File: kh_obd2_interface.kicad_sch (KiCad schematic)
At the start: 8 parts, among them J1 OBD2, Q1 CSD18540Q5B, U1 LM74500-Q1, U2 TVS2700DRV

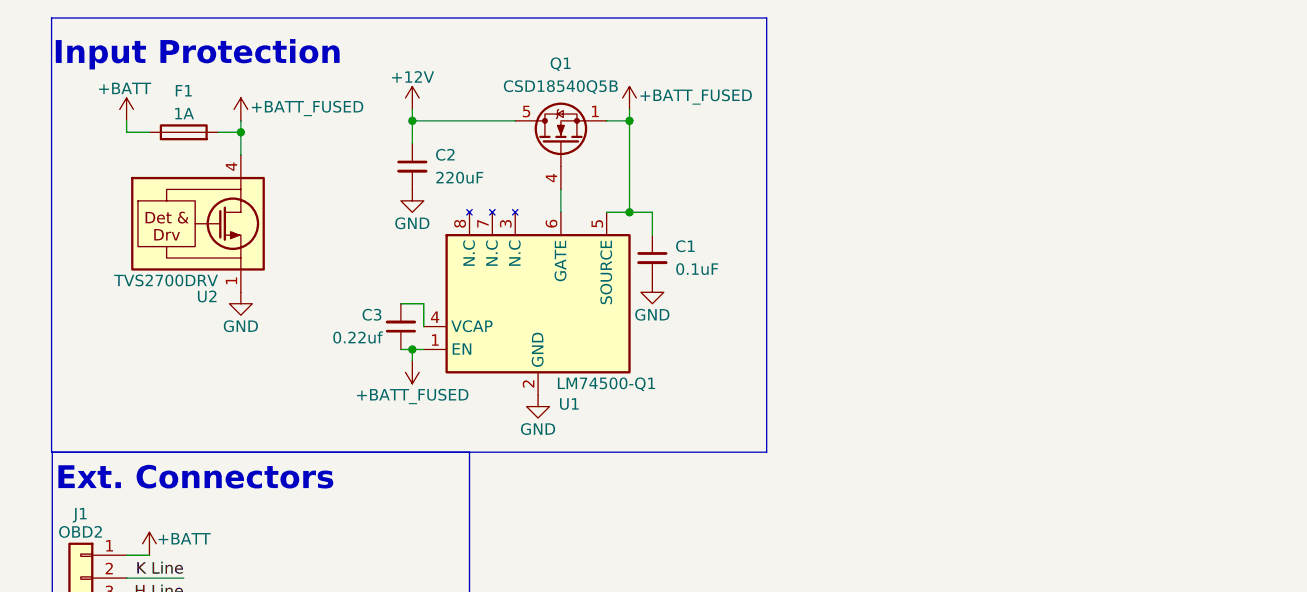
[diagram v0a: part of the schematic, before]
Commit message: Delete backups, add regulator footprint
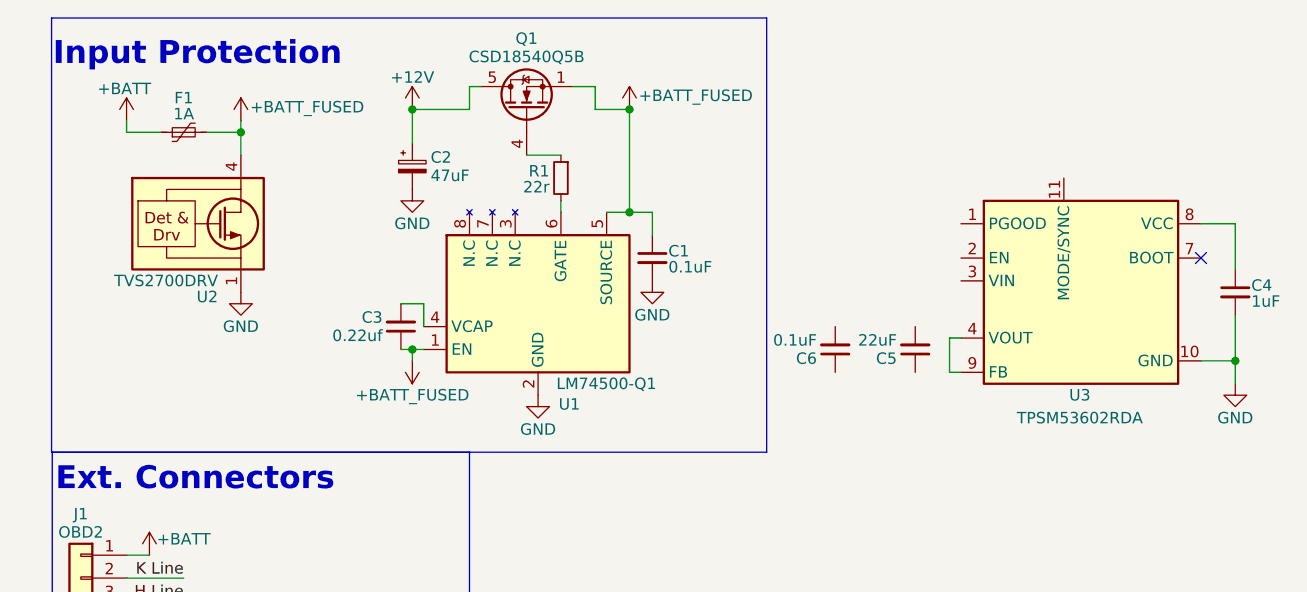
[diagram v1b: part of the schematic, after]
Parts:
- added C4: 1uF, Capacitor_SMD:C_0402_1005Metric, symbol Device:C_Small
- added C5: 22uF, Capacitor_SMD:C_1206_3216Metric, symbol Device:C_Small
- added C6: 0.1uF, Capacitor_SMD:C_1206_3216Metric, symbol Device:C_Small
- added R1: 22r, Resistor_SMD:R_0402_1005Metric, symbol Device:R_Small
- added U3: TPSM53602RDA, TIParts:RDN0011A-MFG, symbol TIParts:TPSM33620S5QRD
- C1, C3: footprint (none) -> Capacitor_SMD:C_0402_1005Metric
- C2: value 220uF -> 47uF; footprint (none) -> Capacitor_SMD:CP_Elec_6.3x5.8; symbol Device:C_Small -> Device:C_Polarized_Small
- F1: footprint (none) -> Fuse:Fuse_1812_4532Metric; symbol Device:Fuse -> Device:Polyfuse_Small
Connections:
- net GND: now also C4.2, U3.10 (GND)
- net at Q1.4 (G): now also R1.1; no longer U1.6 (GATE)
- new net: R1.2, U1.6 (GATE)
- new net: U3.4 (VOUT), U3.9 (FB)
- new net: C4.1, U3.8 (VCC)
- no-connect marks 0 -> 1
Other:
- moved on the sheet: Q1

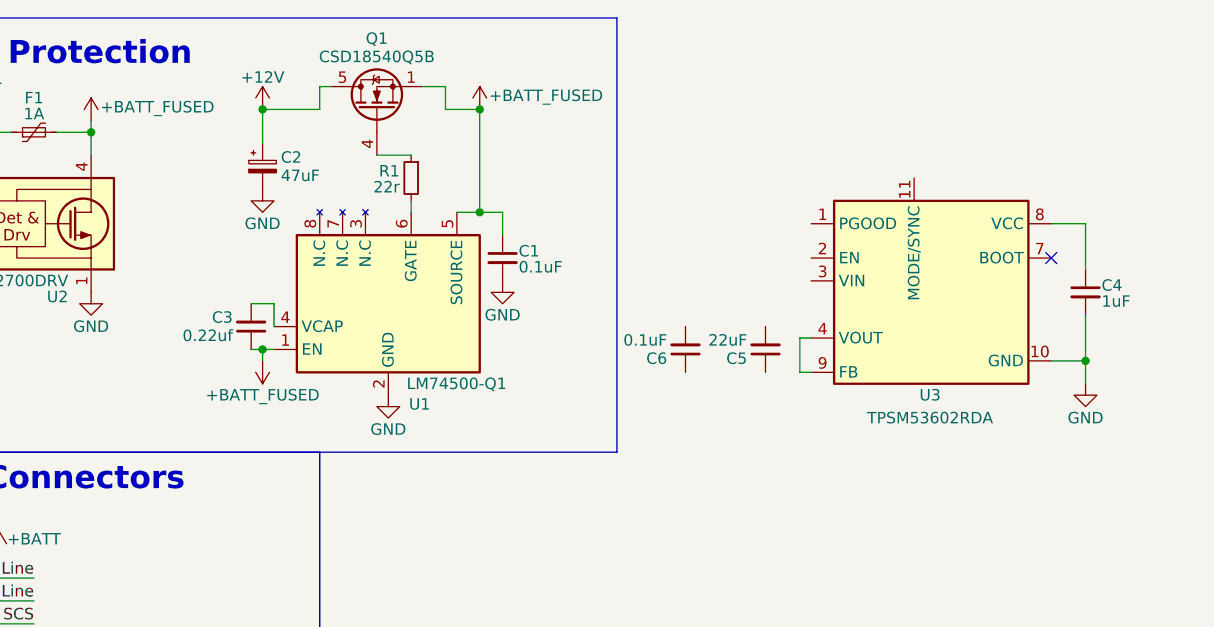
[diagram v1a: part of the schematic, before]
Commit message: Capacitor selections, reg schem done
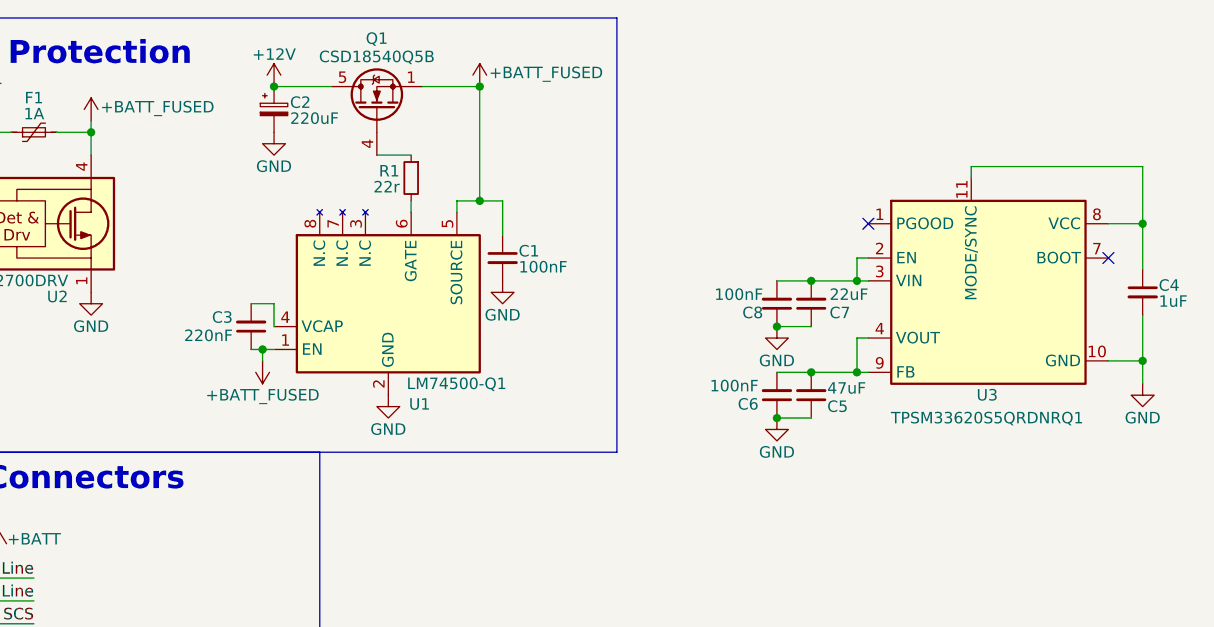
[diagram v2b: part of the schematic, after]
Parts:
- added C6: 100nF, Capacitor_SMD:C_0402_1005Metric, symbol Device:C_Small
- added C7: 22uF, Capacitor_SMD:C_1210_3225Metric, symbol Device:C_Small
- C1: value 0.1uF -> 100nF; Part (none) -> C1005X5R1H104K050BB
- C2: value 47uF -> 220uF; footprint Capacitor_SMD:CP_Elec_6.3x5.8 -> Capacitor_SMD:C_Elec_6.3x5.8; Part (none) -> UWT1H221MNL1GS
- C3: value 0.22uf -> 220nF
- C4: Part (none) -> GRM155R71C104KA88D
- C5: value 22uF -> 47uF; Part (none) -> GRM31CR61A476KE15L
- C8: renamed from C6; value 0.1uF -> 100nF; footprint Capacitor_SMD:C_1206_3216Metric -> Capacitor_SMD:C_0402_1005Metric; Part (none) -> C1005X5R1H104K050BB
- F1: Part (none) -> 1812L110/33MR
- U3: value TPSM53602RDA -> TPSM33620S5QRDNRQ1; footprint TIParts:RDN0011A-MFG -> Package_DFN_QFN:Texas_B3QFN-14-1EP_5x5.5mm_P0.65mm_ThermalVia
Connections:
- net GND: now also C5.1, C8.1, C6.1, C7.1
- net at U3.11 (MODE/SYNC): now also C4.1, U3.8 (VCC)
- net at U3.2 (EN): now also C8.2, U3.3 (VIN), C7.2
- net at U3.4 (VOUT), U3.9 (FB): now also C5.2, C6.2
- no-connect marks 1 -> 2
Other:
- moved on the sheet: C4, C5, C8, U3

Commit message: Some layout
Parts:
- U3: footprint Package_DFN_QFN:Texas_B3QFN-14-1EP_5x5.5mm_P0.65mm_ThermalVia -> TIParts:RDN0011A-MFG
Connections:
- net +12V: now also C7.2, C8.2, U3.2 (EN), U3.3 (VIN)
- net +5V: now reaches C5.2, C6.2, U3.4 (VOUT), U3.9 (FB)
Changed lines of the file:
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@@
+	)
+	(junction
+		(at 115.57 88.9)
+		(diameter 0)
+		(color 0 0 0 0)
 	)
 	(junction
@@
 	(wire
 		(pts
-			(xy 113.03 88.9) (xy 118.11 88.9)
+			(xy 113.03 88.9) (xy 115.57 88.9)
 		)
 		(stroke
@@
 		(pts
 			(xy 119.38 76.2) (xy 118.11 76.2)
+		)
+		(stroke
+			(width 0)
+			(type default)
+		)
+	)
+	(wire
+		(pts
+			(xy 115.57 88.9) (xy 118.11 88.9)
 		)
 		(stroke
@@
 			)
 		)
-		(property "Footprint" "Package_DFN_QFN:Texas_B3QFN-14-1EP_5x5.5mm_P0.65mm_ThermalVia"
+		(property "Footprint" "TIParts:RDN0011A-MFG"
 			(at 99.568 53.594 0)
 			(effects
@@
 	)
 	(symbol
+		(lib_id "power:+5V")
+		(at 115.57 88.9 0)
+		(unit 1)
+		(exclude_from_sim no)
+		(in_bom yes)
+		(on_board yes)
+		(dnp no)
+		(property "Reference" "#PWR016"
+			(at 115.57 92.71 0)
+			(effects
+				(font
+					(size 1.27 1.27)
+				)
+				(hide yes)
+			)
+		)
+		(property "Value" "+5V"
+			(at 115.57 85.09 0)
+			(effects
+				(font
+					(size 1.27 1.27)
+				)
+			)
+		)
+		(property "Footprint" ""
+			(at 115.57 88.9 0)
+			(effects
+				(font
+					(size 1.27 1.27)
+				)
+				(hide yes)
+			)
+		)
+		(property "Datasheet" ""
+			(at 115.57 88.9 0)
+			(effects
+				(font
+					(size 1.27 1.27)
+				)
+				(hide yes)
+			)
+		)
+		(property "Description" "Power symbol creates a global label with name \"+5V\""
+			(at 115.57 88.9 0)
+			(effects
+				(font
+					(size 1.27 1.27)
+				)
+				(hide yes)
+			)
+		)
+		(pin "1"
+		)
+		(instances
+			(project ""
+				(path "/0736e313-8db4-41af-b70d-53af7104d2ca"
+					(reference "#PWR016")
+					(unit 1)
+				)
+			)
+		)
+	)
+	(symbol
 		(lib_id "Device:C_Small")
 		(at 149.86 80.01 0)
@@
 					(unit 1)
 				)
+			)
+		)
+	)
+	(symbol
+		(lib_id "power:+BATT")
+		(at 113.03 78.74 0)
+		(unit 1)
+		(exclude_from_sim no)
+		(in_bom yes)
+		(on_board yes)
+		(dnp no)
+		(property "Reference" "#PWR015"
+			(at 113.03 82.55 0)
+			(effects
+				(font
+					(size 1.27 1.27)
+				)
+				(hide yes)
+			)
+		)
+		(property "Value" "+12V"
+			(at 113.03 75.184 0)
+			(effects
+				(font
+					(size 1.27 1.27)
+				)
+			)
+		)
+		(property "Footprint" ""
+			(at 113.03 78.74 0)
+			(effects
+				(font
+					(size 1.27 1.27)
+				)
+				(hide yes)
+			)
+		)
+		(property "Datasheet" ""
+			(at 113.03 78.74 0)
+			(effects
+				(font
+					(size 1.27 1.27)
+				)
+				(hide yes)
+			)
+		)
+		(property "Description" "Power symbol creates a global label with name \"+BATT\""
+			(at 113.03 78.74 0)
+			(effects
+				(font
+					(size 1.27 1.27)
+				)
+				(hide yes)
+			)
+		)
+		(pin "1"
+		)
+		(instances
+			(project "kh_obd2_interface"
+				(path "/0736e313-8db4-41af-b70d-53af7104d2ca"
+					(reference "#PWR015")
+					(unit 1)
+				)
